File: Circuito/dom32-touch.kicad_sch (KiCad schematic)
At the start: 46 parts, among them J1 MEM2067-02-180-00-A, J2 Poste X 5, J3 MSP3218_LCD, J4 MSP3218_SD, J5 DEBUG, SW1 TactSwitch, U1 ZLDO1117QG33TADICT-ND, U2 PIC32MM0256GPM028-I-SS

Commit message: Se mueve el circuito de directorio
Se mueve el circuito de directorio
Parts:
- added J6: POWER, symbol Connector_Generic:Conn_01x02
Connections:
- net GND: now also J6.2 (Pin_2)
- net at C6.1, C7.1, D6.1 (K)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: no longer J1.4 (VDD), R5.1, R8.1
- net at D4.2 (A): now also J6.1 (Pin_1)
- net at C9.2, D7.1 (K), J3.1 (Pin_1)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: now also J1.4 (VDD), R5.1, R8.1
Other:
- note added: "LCD_RESET"
- moved on the sheet: C9
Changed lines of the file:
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@@
   (junction (at 62.23 109.22) (diameter 0) (color 0 0 0 0)
   )
-  (junction (at 165.1 68.58) (diameter 0) (color 0 0 0 0)
-  )
   (junction (at 43.18 96.52) (diameter 0) (color 0 0 0 0)
   )
@@
   (junction (at 33.02 110.49) (diameter 0) (color 0 0 0 0)
   )
+  (junction (at 189.23 96.52) (diameter 0) (color 0 0 0 0)
+  )
   (junction (at 43.18 78.74) (diameter 0) (color 0 0 0 0)
   )
@@
   (junction (at 142.24 99.06) (diameter 0) (color 0 0 0 0)
   )
+  (junction (at 181.61 81.28) (diameter 0) (color 0 0 0 0)
+  )
   (junction (at 104.14 29.21) (diameter 0) (color 0 0 0 0)
   )
   (junction (at 157.48 139.7) (diameter 0) (color 0 0 0 0)
   )
-  (junction (at 185.42 81.28) (diameter 0) (color 0 0 0 0)
-  )
   (junction (at 152.4 68.58) (diameter 0) (color 0 0 0 0)
   )
@@
   (junction (at 162.56 134.62) (diameter 0) (color 0 0 0 0)
   )
+  (junction (at 180.34 142.24) (diameter 0) (color 0 0 0 0)
+  )
   (junction (at 142.24 68.58) (diameter 0) (color 0 0 0 0)
   )
@@
   (junction (at 157.48 106.68) (diameter 0) (color 0 0 0 0)
   )
-  (junction (at 180.34 142.24) (diameter 0) (color 0 0 0 0)
-  )
   (junction (at 64.77 96.52) (diameter 0) (color 0 0 0 0)
   )
@@
     (stroke (width 0) (type default))
   )
-  (wire (pts (xy 185.42 68.58) (xy 189.23 68.58))
+  (wire (pts (xy 181.61 68.58) (xy 189.23 68.58))
     (stroke (width 0) (type default))
   )
@@
     (stroke (width 0) (type default))
   )
-  (wire (pts (xy 189.23 101.6) (xy 176.53 101.6))
+  (wire (pts (xy 179.07 101.6) (xy 176.53 101.6))
     (stroke (width 0) (type default))
   )
@@
     (stroke (width 0) (type default))
   )
-  (wire (pts (xy 165.1 68.58) (xy 180.34 68.58))
-    (stroke (width 0) (type default))
-  )
-  (wire (pts (xy 189.23 99.06) (xy 189.23 101.6))
+  (wire (pts (xy 179.07 99.06) (xy 179.07 101.6))
     (stroke (width 0) (type default))
   )
@@
     (stroke (width 0) (type default))
   )
+  (wire (pts (xy 38.1 29.21) (xy 48.26 29.21))
+    (stroke (width 0) (type default))
+  )
   (wire (pts (xy 154.94 148.59) (xy 139.7 148.59))
     (stroke (width 0) (type default))
@@
     (stroke (width 0) (type default))
   )
-  (wire (pts (xy 185.42 71.12) (xy 185.42 68.58))
+  (wire (pts (xy 181.61 71.12) (xy 181.61 68.58))
     (stroke (width 0) (type default))
   )
@@
     (stroke (width 0) (type default))
   )
+  (wire (pts (xy 181.61 81.28) (xy 196.85 81.28))
+    (stroke (width 0) (type default))
+  )
   (wire (pts (xy 162.56 134.62) (xy 196.85 134.62))
     (stroke (width 0) (type default))
@@
     (stroke (width 0) (type default))
   )
-  (wire (pts (xy 185.42 78.74) (xy 185.42 81.28))
+  (wire (pts (xy 181.61 78.74) (xy 181.61 81.28))
     (stroke (width 0) (type default))
   )
@@
     (stroke (width 0) (type default))
   )
-  (wire (pts (xy 142.24 81.28) (xy 185.42 81.28))
+  (wire (pts (xy 142.24 81.28) (xy 181.61 81.28))
     (stroke (width 0) (type default))
   )
@@
     (stroke (width 0) (type default))
   )
+  (wire (pts (xy 40.64 31.75) (xy 40.64 36.83))
+    (stroke (width 0) (type default))
+  )
   (wire (pts (xy 182.88 86.36) (xy 196.85 86.36))
     (stroke (width 0) (type default))
@@
     (stroke (width 0) (type default))
   )
-  (wire (pts (xy 189.23 99.06) (xy 196.85 99.06))
+  (wire (pts (xy 179.07 99.06) (xy 196.85 99.06))
     (stroke (width 0) (type default))
   )
@@
     (stroke (width 0) (type default))
   )
+  (wire (pts (xy 38.1 31.75) (xy 40.64 31.75))
+    (stroke (width 0) (type default))
+  )
   (wire (pts (xy 123.19 111.76) (xy 168.91 111.76))
     (stroke (width 0) (type default))
@@
     (stroke (width 0) (type default))
   )
+  (wire (pts (xy 189.23 96.52) (xy 189.23 142.24))
+    (stroke (width 0) (type default))
+  )
   (wire (pts (xy 185.42 91.44) (xy 196.85 91.44))
     (stroke (width 0) (type default))
@@
     (stroke (width 0) (type default))
   )
-  (wire (pts (xy 180.34 68.58) (xy 180.34 142.24))
+  (wire (pts (xy 189.23 142.24) (xy 180.34 142.24))
     (stroke (width 0) (type default))
   )
@@
   )
   (wire (pts (xy 86.36 40.64) (xy 88.9 40.64))
-    (stroke (width 0) (type default))
-  )
-  (wire (pts (xy 185.42 81.28) (xy 196.85 81.28))
     (stroke (width 0) (type default))
   )
@@
     (effects (font (size 1.27 1.27)) (justify left bottom))
   )
+  (text "LCD_DC" (at 81.28 116.84 0)
+    (effects (font (size 1.27 1.27)) (justify left bottom))
+  )
   (text "LCD_CS" (at 124.46 111.76 0)
     (effects (font (size 1.27 1.27)) (justify left bottom))
@@
   )
   (text "LCD_CS" (at 204.47 85.09 0)
+    (effects (font (size 1.27 1.27)) (justify left bottom))
+  )
+  (text "LCD_RESET" (at 78.74 120.65 0)
     (effects (font (size 1.27 1.27)) (justify left bottom))
   )
@@
         (path "/52c02980-b5ea-450b-8d27-915fdca3d27d"
           (reference "U1") (unit 1)
+        )
+      )
+    )
+  )
+  (symbol (lib_id "power:GND") (at 40.64 36.83 0) (unit 1)
+    (in_bom yes) (on_board yes) (dnp no)
+    (property "Reference" "#PWR012" (at 40.64 43.18 0)
+      (effects (font (size 1.27 1.27)) hide)
+    )
+    (property "Value" "GND" (at 40.767 41.2242 0)
+      (effects (font (size 1.27 1.27)) hide)
+    )
+    (property "Footprint" "" (at 40.64 36.83 0)
+      (effects (font (size 1.27 1.27)) hide)
+    )
+    (property "Datasheet" "" (at 40.64 36.83 0)
+      (effects (font (size 1.27 1.27)) hide)
+    )
+    (pin "1")
+    (instances
+      (project "dom32-touch"
+        (path "/52c02980-b5ea-450b-8d27-915fdca3d27d"
+          (reference "#PWR012") (unit 1)
         )
       )
@@
     )
   )
+  (symbol (lib_id "Connector_Generic:Conn_01x02") (at 33.02 29.21 0) (mirror y) (unit 1)
+    (in_bom yes) (on_board yes) (dnp no)
+    (property "Reference" "J6" (at 34.29 34.29 0)
+      (effects (font (size 1.27 1.27)) (justify left))
+    )
+    (property "Value" "POWER" (at 34.29 36.83 0)
+      (effects (font (size 1.27 1.27)) (justify left))
+    )
+    (property "Footprint" "" (at 33.02 29.21 0)
+      (effects (font (size 1.27 1.27)) hide)
+    )
+    (property "Datasheet" "~" (at 33.02 29.21 0)
+      (effects (font (size 1.27 1.27)) hide)
+    )
+    (pin "2")
+    (pin "1")
+    (instances
+      (project "dom32-touch"
+        (path "/52c02980-b5ea-450b-8d27-915fdca3d27d"
+          (reference "J6") (unit 1)
+        )
+      )
+    )
+  )
   (symbol (lib_id "Device:R") (at 74.93 127 180) (unit 1)
     (in_bom yes) (on_board yes) (dnp no)
@@
     )
   )
-  (symbol (lib_id "Device:C") (at 185.42 74.93 180) (unit 1)
-    (in_bom yes) (on_board yes) (dnp no)
-    (property "Reference" "C9" (at 193.04 69.85 0)
-      (effects (font (size 1.27 1.27)) (justify left))
-    )
-    (property "Value" "100nf / 50v" (at 203.2 72.39 0)
-      (effects (font (size 1.27 1.27)) (justify left))
-    )
-    (property "Footprint" "Capacitor_SMD:C_0805_2012Metric_Pad1.18x1.45mm_HandSolder" (at 184.4548 71.12 0)
-      (effects (font (size 1.27 1.27)) hide)
-    )
-    (property "Datasheet" "~" (at 185.42 74.93 0)
-      (effects (font (size 1.27 1.27)) hide)
-    )
+  (symbol (lib_id "Device:C") (at 181.61 74.93 180) (unit 1)
+    (in_bom yes) (on_board yes) (dnp no)
+    (property "Reference" "C9" (at 189.23 69.85 0)
+      (effects (font (size 1.27 1.27)) (justify left))
+    )
+    (property "Value" "100nf / 50v" (at 199.39 72.39 0)
+      (effects (font (size 1.27 1.27)) (justify left))
+    )
+    (property "Footprint" "Capacitor_SMD:C_0805_2012Metric_Pad1.18x1.45mm_HandSolder" (at 180.6448 71.12 0)
+      (effects (font (size 1.27 1.27)) hide)
+    )
+    (property "Datasheet" "~" (at 181.61 74.93 0)
+      (effects (font (size 1.27 1.27)) hide)
+    )

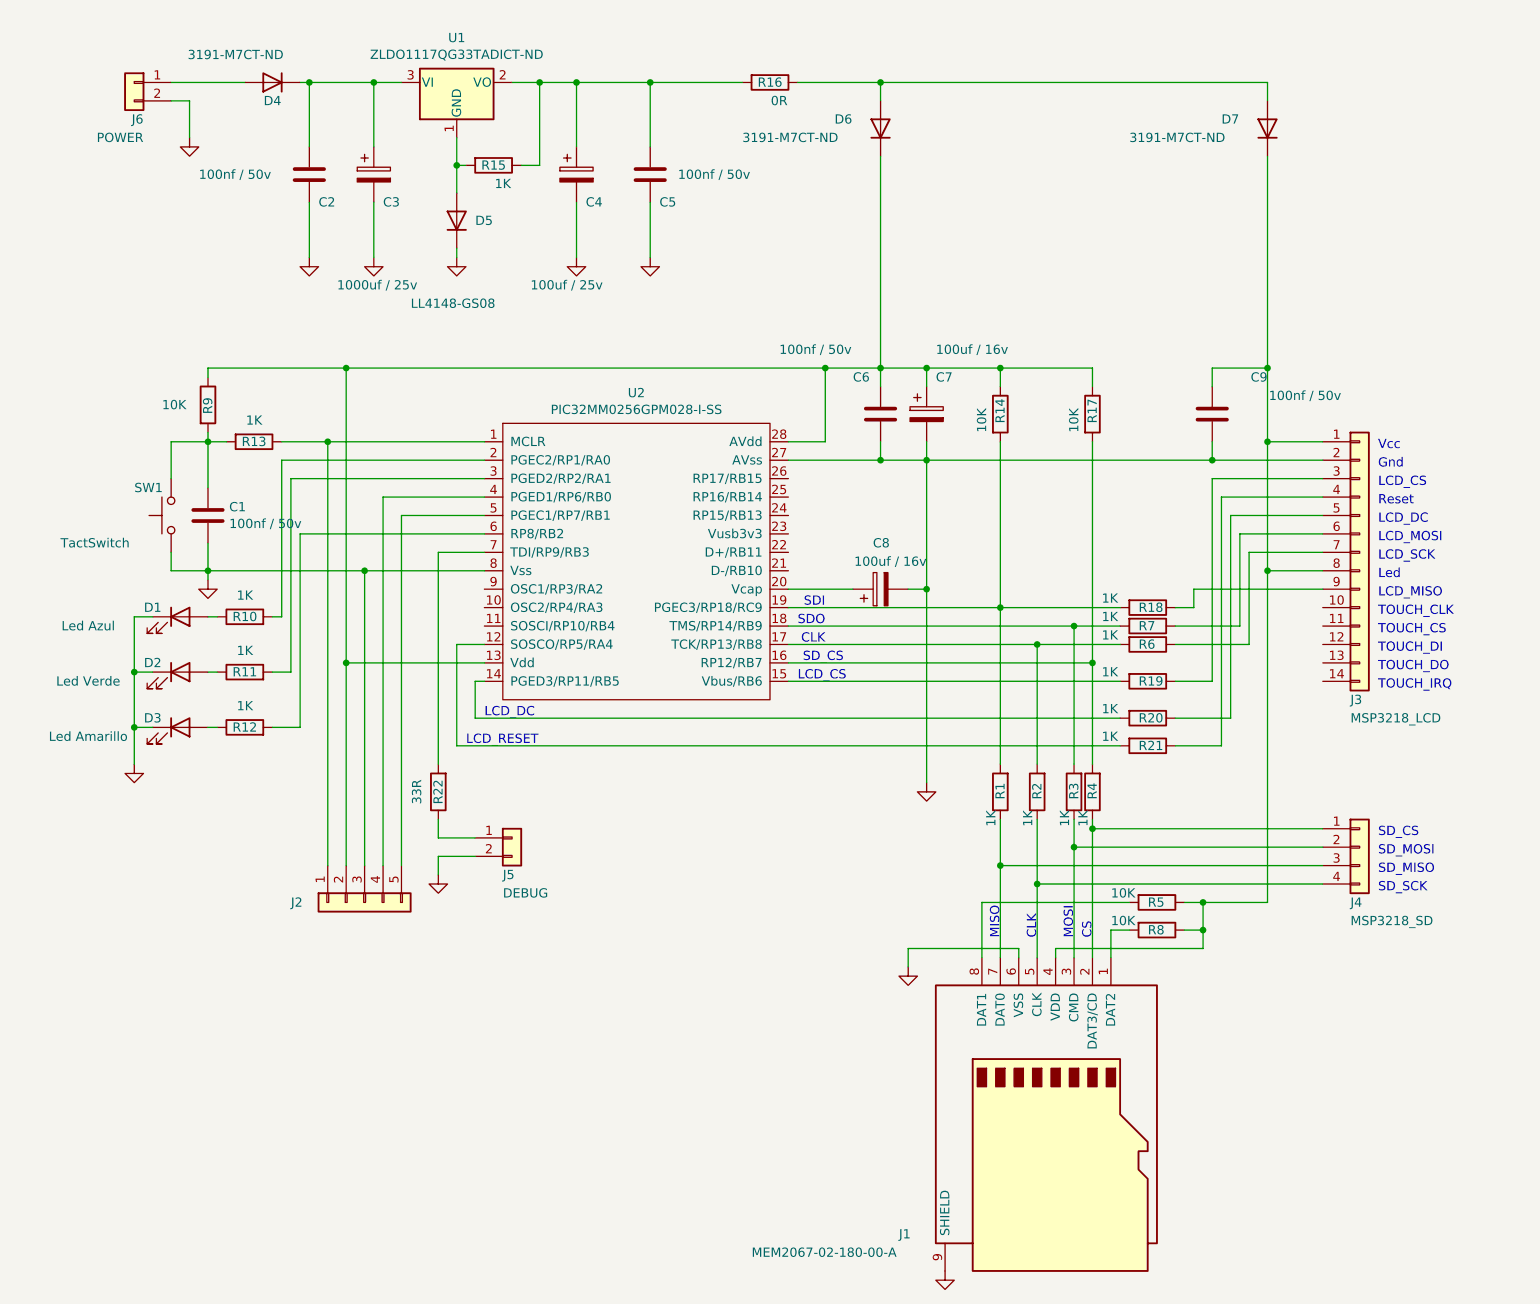
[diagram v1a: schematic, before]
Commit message: No funciona
El display utilizado necesita alimentarse con 5v y las señales en el mismo valor. El uso de open collector con resistencias de 10k a 5v no alcanzó
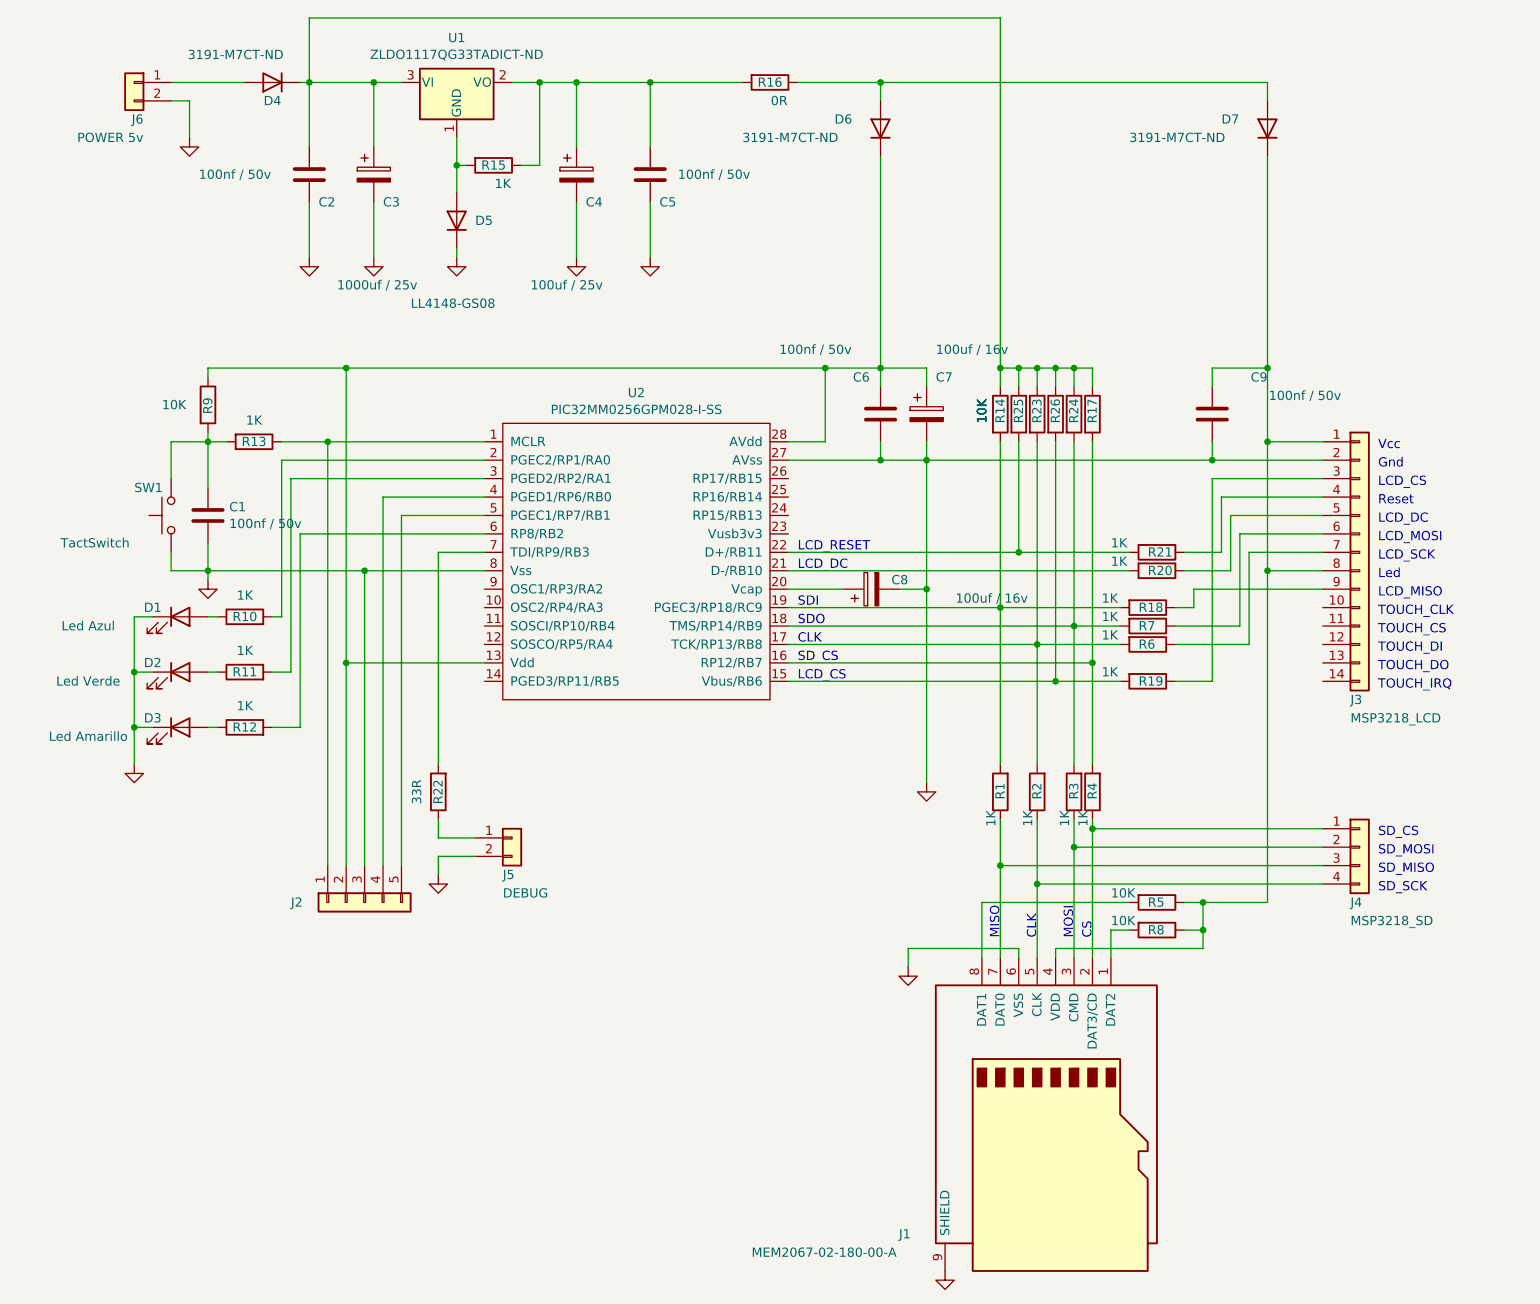
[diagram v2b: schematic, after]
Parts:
- added R23, R24, R25, R26: 10K, Resistor_SMD:R_0805_2012Metric_Pad1.20x1.40mm_HandSolder, symbol Device:R
- J6: value POWER -> POWER 5v
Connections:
- net at C6.1, C7.1, D6.1 (K)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: no longer R14.1, R17.1
- net at C2.1, C3.1, D4.1 (K)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: now also R14.1, R17.1, R23.1, R24.1, R25.1, R26.1
- net at R3.2, R7.2, U2.18 (TMS/RP14/RB9): now also R24.2
- net at R21.2: now also U2.22 (D+/RB11), R25.2; no longer U2.12 (SOSCO/RP5/RA4)
- net at U2.14 (PGED3/RP11/RB5): no longer R20.2
- net at R19.2, U2.15 (Vbus/RB6): now also R26.2
- net at R2.2, R6.2, U2.17 (TCK/RP13/RB8): now also R23.2
- net at U2.21 (D-/RB10): now also R20.2
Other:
- moved on the sheet: C8, R20, R21
